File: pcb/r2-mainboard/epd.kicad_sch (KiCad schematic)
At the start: 8 parts, among them J6 FPC-05F-50PH20

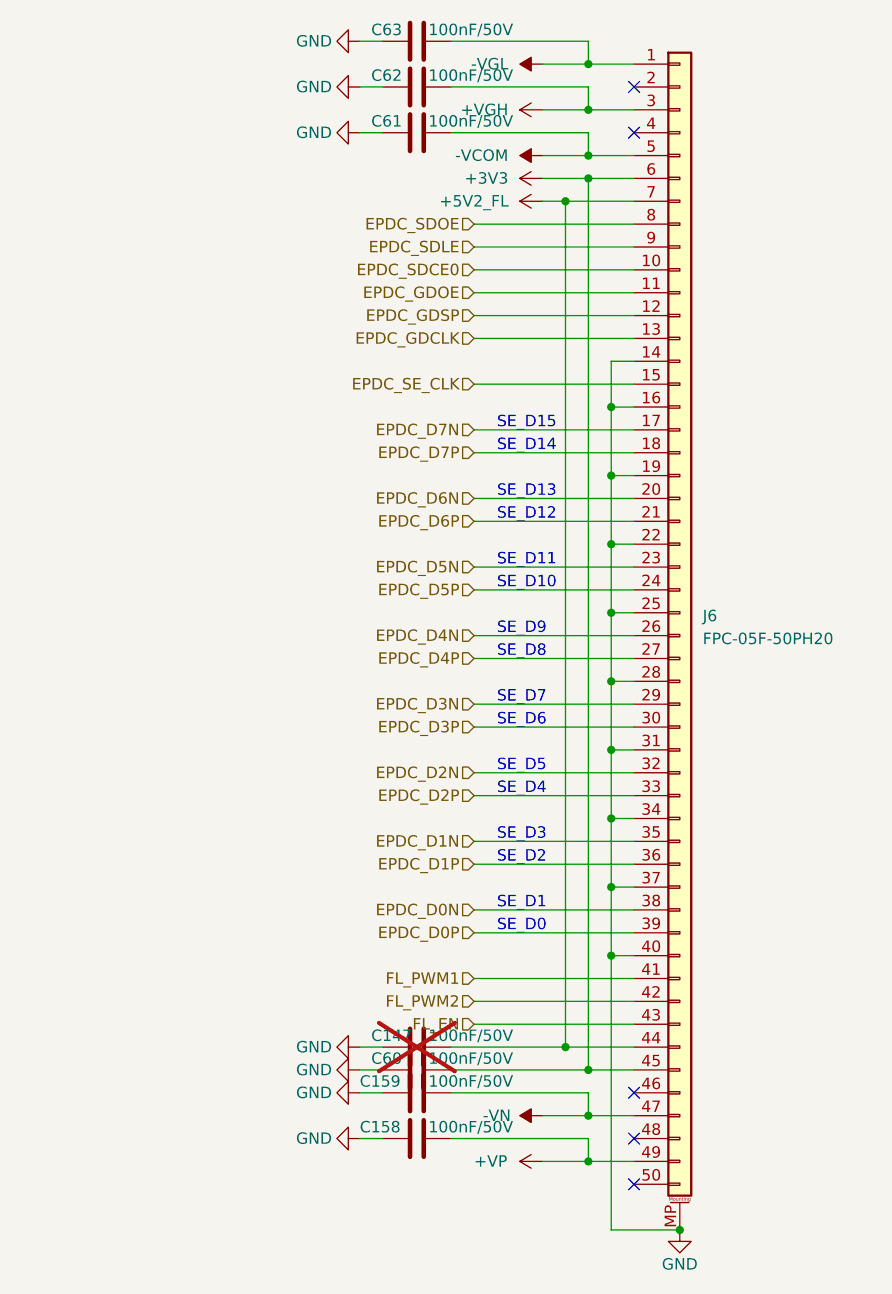
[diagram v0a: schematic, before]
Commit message: change layout and reduce board size + add second usb host only
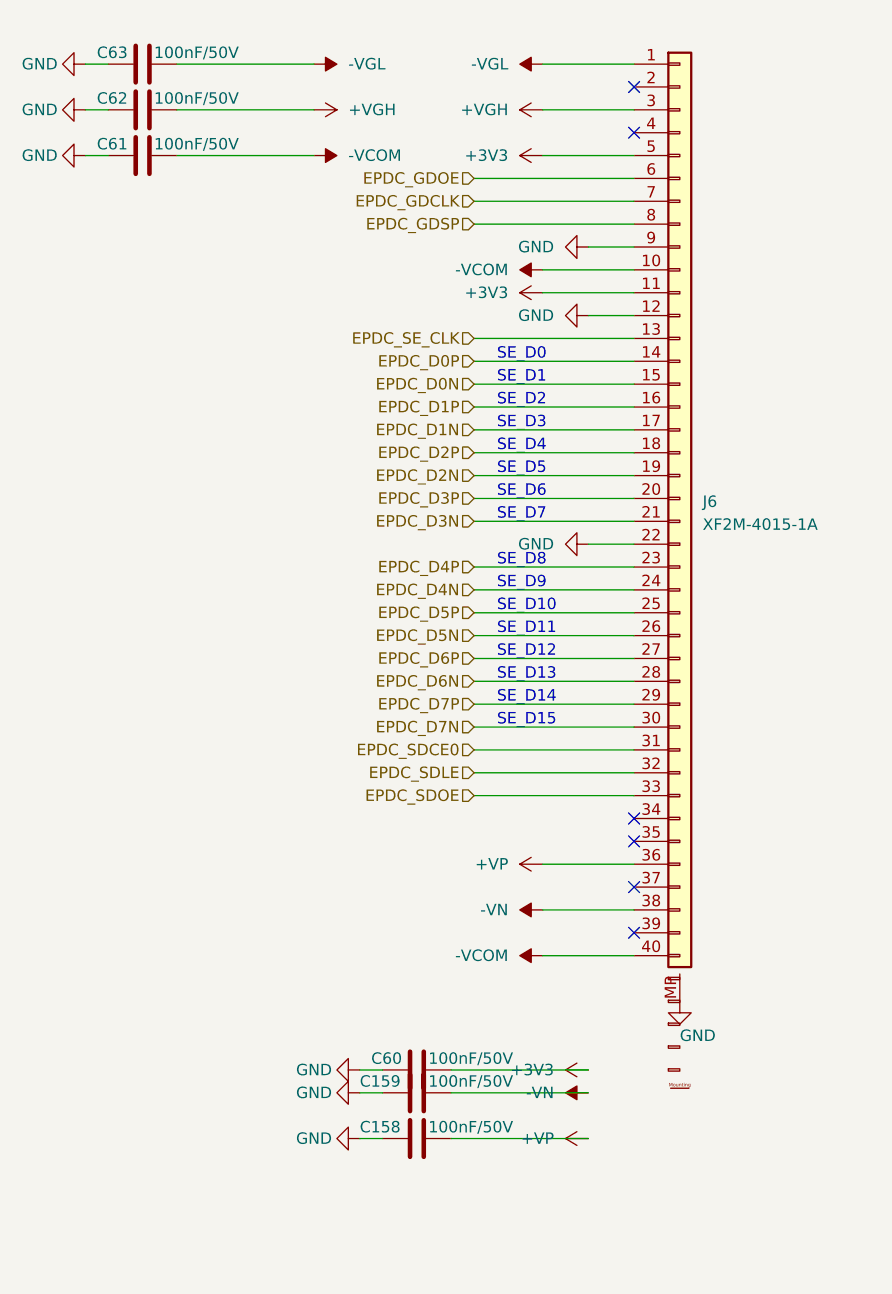
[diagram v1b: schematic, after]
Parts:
- removed C147: 100nF/50V, Capacitor_SMD:C_0402_1005Metric, symbol Device:C
- J6: value FPC-05F-50PH20 -> XF2M-4015-1A; footprint footprints:Xunpu_FPC-05F-50PH20_1x50-1MP_P0.50mm_Horizontal -> r2:Omron_XF2M-4015-1A_1x40-1MP_P0.5mm_Horizontal_Mirrored; symbol Connector_Generic_MountingPin:Conn_01x50_MountingPin -> Connector_Generic_MountingPin:Conn_01x40_MountingPin; LCSC C2856813 -> C225713; MPN FPC-05F-50PH20 -> XF2M-4015-1A; Manufacturer XUNPU -> Omron
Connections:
- net +3V3: now also J6.11 (Pin_11), J6.5 (Pin_5); no longer J6.45 (Pin_45), J6.6 (Pin_6)
- net +VP: now also J6.36 (Pin_36); no longer J6.49 (Pin_49)
- net -VCOM: now also J6.10 (Pin_10), J6.40 (Pin_40); no longer J6.5 (Pin_5)
- net -VN: now also J6.38 (Pin_38); no longer J6.47 (Pin_47)
- net EPDC_D0N: now also J6.15 (Pin_15); no longer J6.38 (Pin_38)
- net EPDC_D0P: now also J6.14 (Pin_14); no longer J6.39 (Pin_39)
- net EPDC_D1N: now also J6.17 (Pin_17); no longer J6.35 (Pin_35)
- net EPDC_D1P: now also J6.16 (Pin_16); no longer J6.36 (Pin_36)
- net EPDC_D2N: now also J6.19 (Pin_19); no longer J6.32 (Pin_32)
- net EPDC_D2P: now also J6.18 (Pin_18); no longer J6.33 (Pin_33)
- net EPDC_D3N: now also J6.21 (Pin_21); no longer J6.29 (Pin_29)
- net EPDC_D3P: now also J6.20 (Pin_20); no longer J6.30 (Pin_30)
- net EPDC_D4N: now also J6.24 (Pin_24); no longer J6.26 (Pin_26)
- net EPDC_D4P: now also J6.23 (Pin_23); no longer J6.27 (Pin_27)
- net EPDC_D5N: now also J6.26 (Pin_26); no longer J6.23 (Pin_23)
- net EPDC_D5P: now also J6.25 (Pin_25); no longer J6.24 (Pin_24)
- net EPDC_D6N: now also J6.28 (Pin_28); no longer J6.20 (Pin_20)
- net EPDC_D6P: now also J6.27 (Pin_27); no longer J6.21 (Pin_21)
- net EPDC_D7N: now also J6.30 (Pin_30); no longer J6.17 (Pin_17)
- net EPDC_D7P: now also J6.29 (Pin_29); no longer J6.18 (Pin_18)
- net EPDC_GDCLK: now also J6.7 (Pin_7); no longer J6.13 (Pin_13)
- net EPDC_GDOE: now also J6.6 (Pin_6); no longer J6.11 (Pin_11)
- net EPDC_GDSP: now also J6.8 (Pin_8); no longer J6.12 (Pin_12)
- net EPDC_SDCE0: now also J6.31 (Pin_31); no longer J6.10 (Pin_10)
- net EPDC_SDLE: now also J6.32 (Pin_32); no longer J6.9 (Pin_9)
- net EPDC_SDOE: now also J6.33 (Pin_33); no longer J6.8 (Pin_8)
- net EPDC_SE_CLK: now also J6.13 (Pin_13); no longer J6.15 (Pin_15)
- net GND: now also J6.12 (Pin_12), J6.9 (Pin_9); no longer J6.14 (Pin_14), J6.16 (Pin_16), J6.19 (Pin_19), J6.25 (Pin_25), J6.28 (Pin_28), J6.31 (Pin_31), J6.34 (Pin_34), J6.37 (Pin_37), J6.40 (Pin_40)
- removed net +5V2_FL: J6.44 (Pin_44), J6.7 (Pin_7)
- removed net FL_EN: J6.43 (Pin_43)
- removed net FL_PWM1: J6.41 (Pin_41)
- removed net FL_PWM2: J6.42 (Pin_42)
- no-connect marks 5 -> 6
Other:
- moved on the sheet: C61, C62, C63
